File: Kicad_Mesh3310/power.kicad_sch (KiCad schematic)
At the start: 37 parts, among them J4 Conn_01x05_Pin, J9 Battery, Q8 BSS138, Q9 BSS138, SW18 POWER ON/OFF, U14 TPS63031DSK, U3 BQ24074RGT, U9 MAX16054

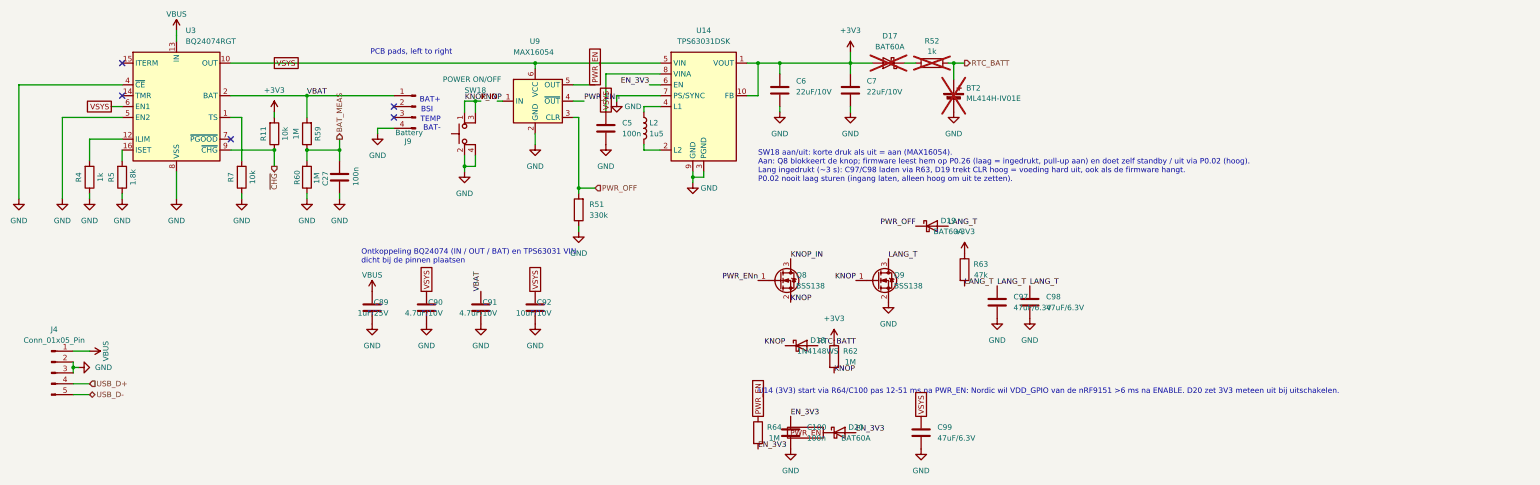
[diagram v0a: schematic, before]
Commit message: Rev. F + G: controleronde, TPS3420 aan/uit-knop, FLASH_CS pull-up, RF4 DNP, U.FL-variant LoRa
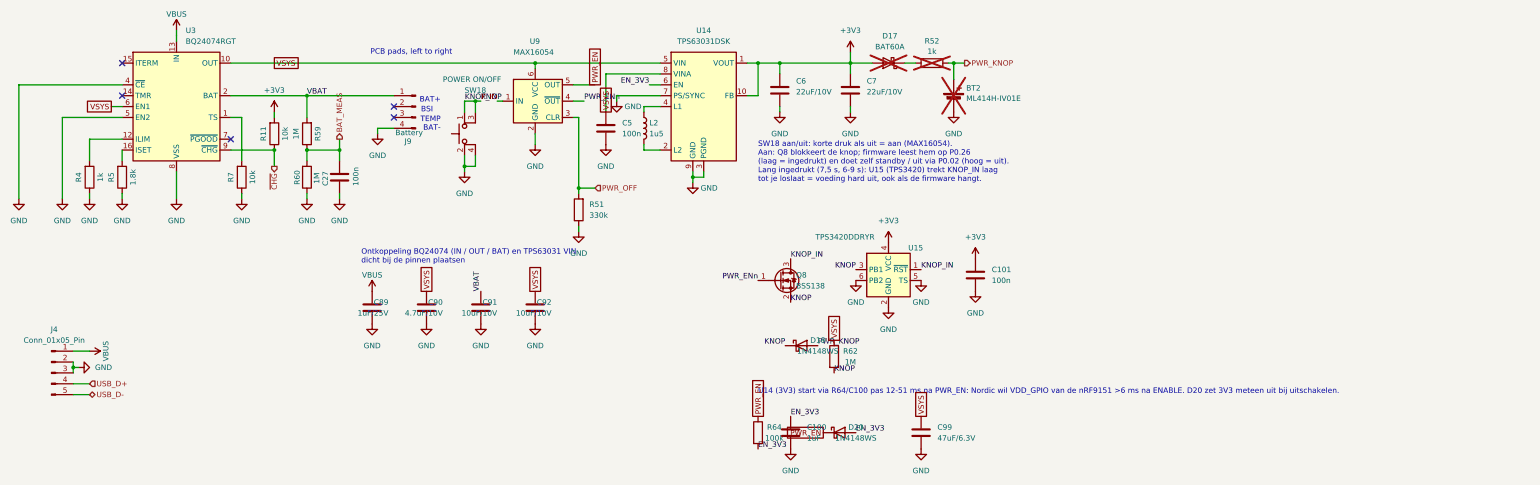
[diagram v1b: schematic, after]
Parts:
- removed C97, C98: 47uF/6.3V, Capacitor_SMD:C_0805_2012Metric, symbol Device:C
- removed D19: BAT60A, Diode_SMD:D_SOD-323, symbol Diode:BAT60A
- removed Q9: BSS138, Package_TO_SOT_SMD:SOT-23, symbol Transistor_FET:BSS138
- removed R63: 47k, Resistor_SMD:R_0201_0603Metric, symbol Device:R
- added C101: 100n, Capacitor_SMD:C_0201_0603Metric, symbol Device:C
- added U15: TPS3420DDRYR, Package_SON:Texas_USON-6_1x1.45mm_P0.5mm_SMD, symbol Parts:TPS3420
- C100: value 100n -> 1uF; footprint Capacitor_SMD:C_0201_0603Metric -> Capacitor_SMD:C_0402_1005Metric; LCSC C408130 -> C52923
- C91: value 4.7uF/10V -> 10uF/10V; LCSC C19666 -> C19702
- D20: value BAT60A -> 1N4148WS; LCSC C5355496 -> C2128
- R64: value 1M -> 100k; LCSC C473482 -> C3152012
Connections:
- net +3V3: now also C101.2, U15.4 (VCC); no longer R62.1
- net GND: now also C101.1, U15.2 (GND), U15.5 (TS), U15.6 (PB2)
- net KNOP: now also U15.3 (PB1)
- net KNOP_IN: now also U15.1 (~{RST})
- net VSYS: now also R62.1
- net RTC_BATT renamed PWR_KNOP
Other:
- note added: "SW18 aan/uit: korte druk als uit = aan (MAX16054). Aan: Q8 blokkeert de knop; firmware leest hem op P0.26 (laag = ingedrukt) en doet zelf standby / uit via P0.02 (hoog = uit). Lang ingedrukt (7,5 s, 6-9 s): U15 (TPS3420) trekt KNOP_IN laag tot je loslaat = voeding hard uit, ook als de firmware hangt."
- note removed: "SW18 aan/uit: korte druk als uit = aan (MAX16054). Aan: Q8 blokkeert de knop; firmware leest hem op P0.26 (laag = ingedrukt, pull-up aan) en doet zelf standby / uit via P0.02 (hoog). Lang ingedrukt (~3 s): C97/C98 laden via R63, D19 trekt CLR hoog = voeding hard uit, ook als de firmware hangt. P0.02 nooit laag sturen (ingang laten, alleen hoog om uit te zetten)."

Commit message: Onderdelen die JLC niet had vervangen, JLC-uploadbestanden toegevoegd
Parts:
- R51: LCSC C270349 -> C142017
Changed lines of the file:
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@@
 			)
 		)
-		(property "LCSC" "C270349"
+		(property "LCSC" "C142017"
 			(at 170.688 114.3 90)
 			(effects
